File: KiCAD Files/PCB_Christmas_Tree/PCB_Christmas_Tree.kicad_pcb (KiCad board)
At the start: 2 copper layers, 207.1 x 98.8 mm, 75 parts, among them J1 Conn_01x03_Pin, J2 CR2032, J3 Conn_01x04_Pin, J4 Conn_01x04_Pin, J5 Conn_01x04_Pin, J7 Conn_01x04_Pin, Q1 AO3401A, Q2 AO3401A, Q3 AO3401A, Q4 BC817, Q5 AO3401A, SW1 SW_Omron_B3FS, U1 ATtiny402-SS

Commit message: v2 added
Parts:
- Q1: renamed from Q2; footprint Package_TO_SOT_SMD:SOT-23 -> Package_TO_SOT_SMD:SOT-323_SC-70_Handsoldering
- Q2: renamed from Q3; footprint Package_TO_SOT_SMD:SOT-23 -> Package_TO_SOT_SMD:SOT-323_SC-70_Handsoldering
- Q3: renamed from Q1; footprint Package_TO_SOT_SMD:SOT-23 -> Package_TO_SOT_SMD:SOT-323_SC-70_Handsoldering
- Q5: footprint Package_TO_SOT_SMD:SOT-23 -> Package_TO_SOT_SMD:SOT-323_SC-70_Handsoldering
- moved R5 0.13 mm to (102.6, 137.0)
- renumbered D6 to D10, D7 to D11, D8 to D12, D9 to D13, D10 to D14, D11 to D15, D12 to D16, D13 to D17, D14 to D18, D15 to D19, D23 to D2, D16 to D20, D17 to D21, D19 to D22, D20 to D23, D25 to D24, D24 to D25, D22 to D3, D21 to D4, D18 to D5, D2 to D6, D3 to D7, D4 to D8, D5 to D9, J2 to J1, J1 to J2, J7 to J3, J3 to J5, J5 to J6, R2 to R1, R7 to R10, R8 to R11, R9 to R12, R10 to R13, R11 to R14, R12 to R15, R13 to R16, R14 to R17, R15 to R18, R16 to R19, Rq1 to R2, R17 to R20, R18 to R21, R19 to R22, R20 to R23, R21 to R24, R22 to R25, R24 to R26, R25 to R27, R30 to R28, R1 to R3, R28 to R6, R27 to R7, R26 to R8, R23 to R9
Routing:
- net /LED_Power_3: track 356.2 -> 349.5 mm, vias 26 -> 24
- net /LED_Power_1: track 354.1 -> 357.6 mm
- net VDD: track 64.3 -> 66.8 mm
- net +BATT: track 34.1 -> 35.1 mm
- net Net-(Q5-G): track 5.86 -> 5.21 mm
- net Net-(D5-K): track 4.84 -> 5.43 mm
- net /LED_Power_2: track 344.6 -> 344.7 mm, vias 23 -> 22
- net GND: vias 63 -> 172
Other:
- board text added: "GND"
- board text added: "UPDI"
- board text added: "VDD"

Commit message: PCB update
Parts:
- added G***: LOGO, LOGO, F.Cu at (190.0, 130.0)
- added G***: LOGO, LOGO, B.Cu at (188.0, 134.0)
- R1, R10, R11, R12, R13, R14, R15, R16, R17, R18, R19, R2, R20, R21, R22, R23, R24, R25, R26, R27, R28, R29, R3, R4, R5, R6, R7, R8, R9: footprint Resistor_SMD:R_0603_1608Metric_Pad0.98x0.95mm_HandSolder -> Resistor_SMD:R_0805_2012Metric_Pad1.20x1.40mm_HandSolder
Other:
- outline, holes or cut-outs redrawn

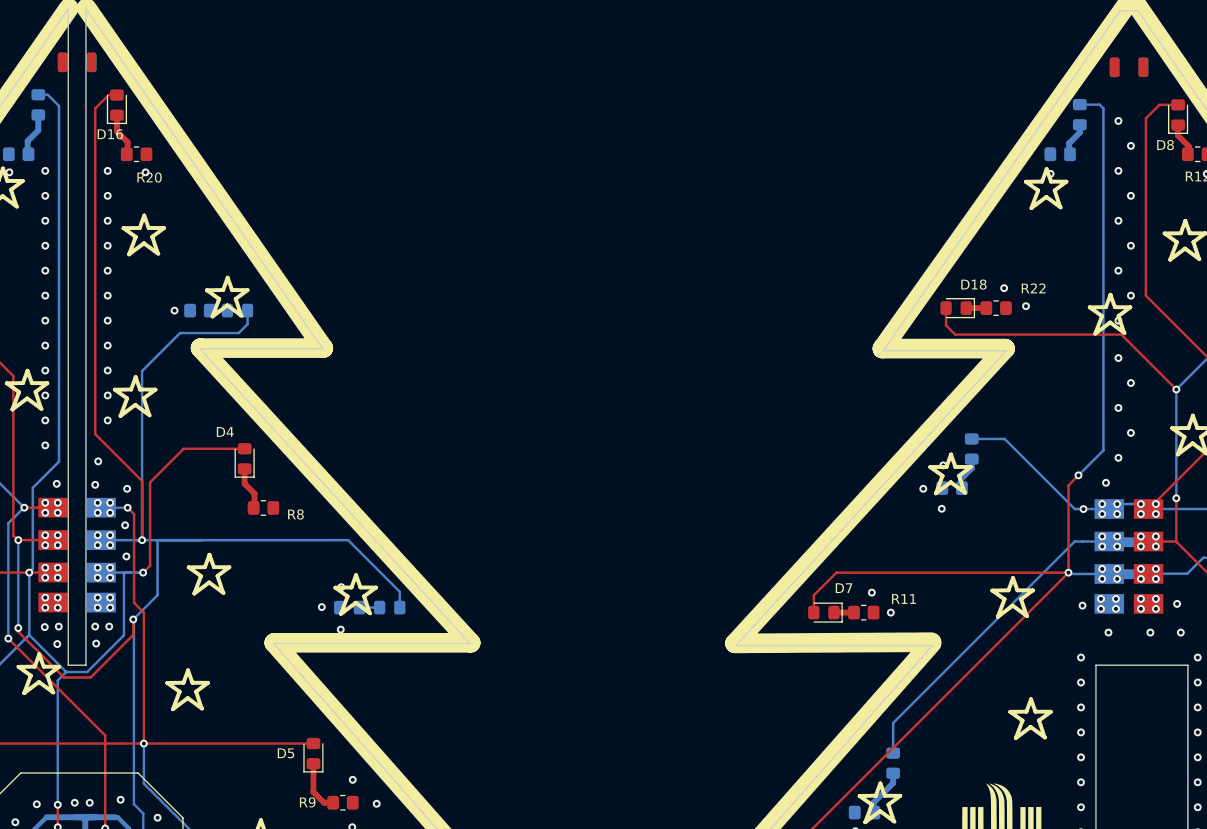
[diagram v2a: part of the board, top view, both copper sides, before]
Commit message: dodano przelotki
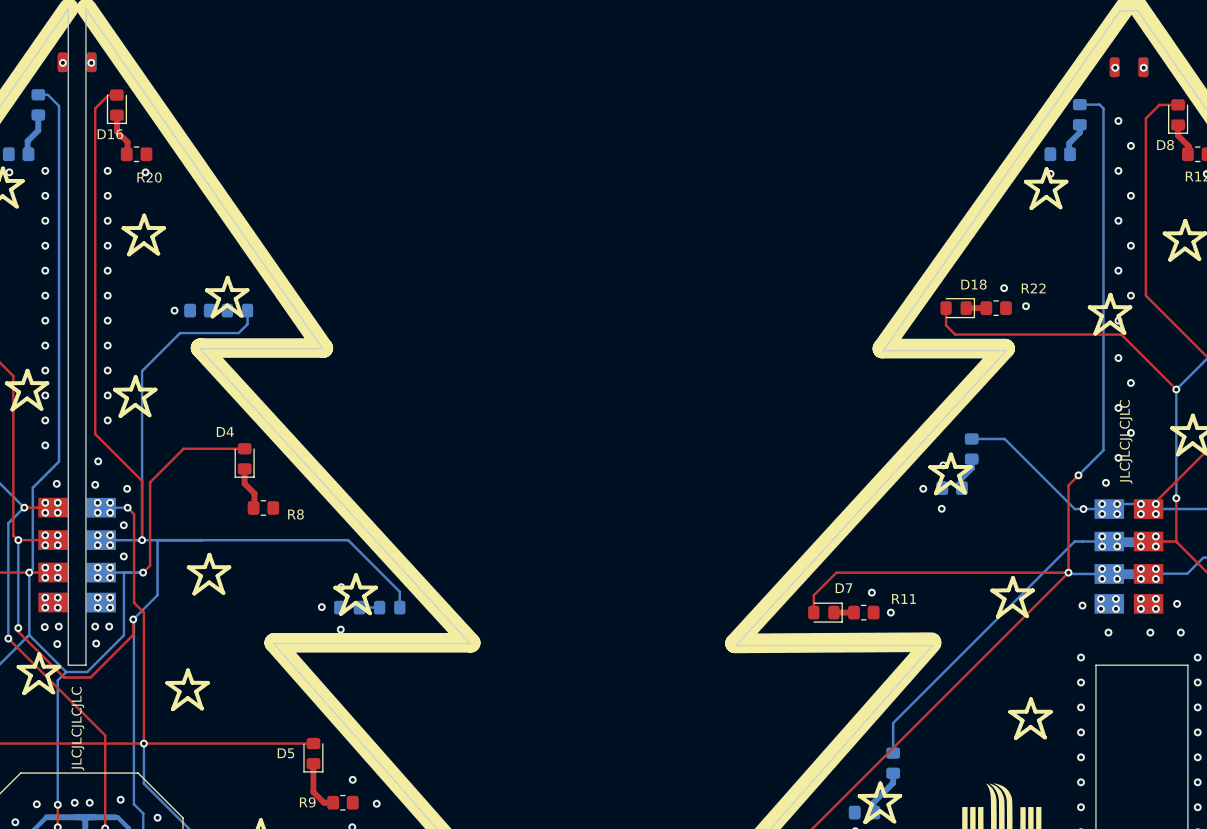
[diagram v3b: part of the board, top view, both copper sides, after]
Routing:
- net (no net): vias 0 -> 4
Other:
- board text added: "JLCJLCJLCJLC"
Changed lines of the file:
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@@
+    (effects (font (size 1 1) (thickness 0.15)) (justify left bottom))
+  )
+  (gr_text "JLCJLCJLCJLC" (at 96.52 120.65 90) (layer "F.SilkS")
     (effects (font (size 1 1) (thickness 0.15)) (justify left bottom))
   )
@@
     (effects (font (size 1 1) (thickness 0.15)) (justify left bottom))
   )
+  (gr_text "JLCJLCJLCJLC" (at 203.2 91.44 90) (layer "F.SilkS")
+    (effects (font (size 1 1) (thickness 0.15)) (justify left bottom))
+  )
   (gr_text "GND\n" (at 110.49 137.16 90) (layer "F.SilkS")
     (effects (font (size 1 1) (thickness 0.15)) (justify left bottom))
   )
+  (via (at 97.4 48.7) (size 0.8) (drill 0.4) (layers "F.Cu" "B.Cu") (net 0))
+  (via (at 201.6 49.2) (size 0.8) (drill 0.4) (layers "F.Cu" "B.Cu") (net 0))
+  (via (at 94.5 48.7) (size 0.8) (drill 0.4) (layers "F.Cu" "B.Cu") (net 0))
+  (via (at 204.5 49.2) (size 0.8) (drill 0.4) (layers "F.Cu" "B.Cu") (net 0))
   (segment (start 94.696 132.6455) (end 95.4005 133.35) (width 0.45) (layer "B.Cu") (net 1))
   (segment (start 94.696 130.6945) (end 94.696 132.6455) (width 0.45) (layer "B.Cu") (net 1))
@@
   (via (at 124.0028 121.666) (size 0.8) (drill 0.4) (layers "F.Cu" "B.Cu") (free) (net 24))
   (via (at 99.314 104.14) (size 0.8) (drill 0.4) (layers "F.Cu" "B.Cu") (net 24))
-  (via (at 100.838 95.758) (size 0.8) (drill 0.4) (layers "F.Cu" "B.Cu") (free) (net 24))
+  (via (at 100.7 95.758) (size 0.8) (drill 0.4) (layers "F.Cu" "B.Cu") (free) (net 24))
   (via (at 210 111.76) (size 0.8) (drill 0.4) (layers "F.Cu" "B.Cu") (free) (net 24))
   (via (at 198.12 137.16) (size 0.8) (drill 0.4) (layers "F.Cu" "B.Cu") (free) (net 24))
@@
   (via (at 210 114.3) (size 0.8) (drill 0.4) (layers "F.Cu" "B.Cu") (free) (net 24))
   (via (at 81.1276 131.5212) (size 0.8) (drill 0.4) (layers "F.Cu" "B.Cu") (free) (net 24))
-  (via (at 100.965 98.933) (size 0.8) (drill 0.4) (layers "F.Cu" "B.Cu") (free) (net 24))
+  (via (at 100.7 98.933) (size 0.8) (drill 0.4) (layers "F.Cu" "B.Cu") (free) (net 24))
   (via (at 230.9368 121.92) (size 0.8) (drill 0.4) (layers "F.Cu" "B.Cu") (free) (net 24))
   (via (at 200.152 104.267) (size 0.8) (drill 0.4) (layers "F.Cu" "B.Cu") (net 24))

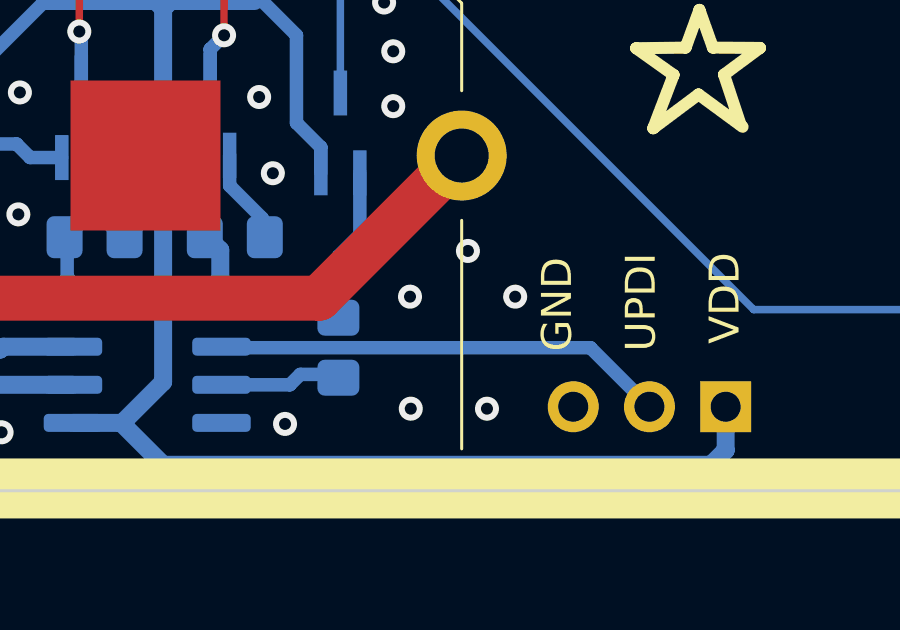
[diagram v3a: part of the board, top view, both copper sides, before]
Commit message: zmiana pinoutu zlacza UPDI
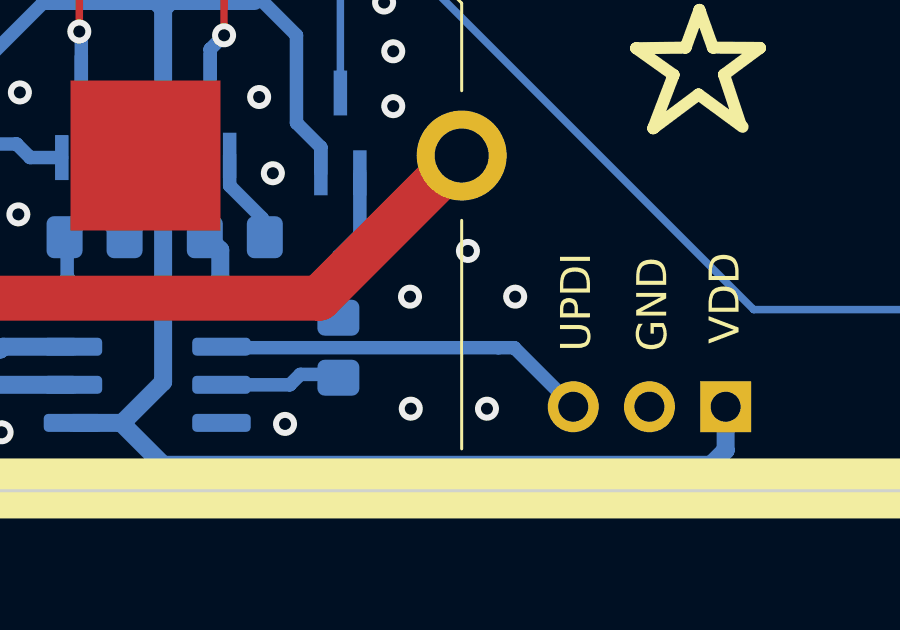
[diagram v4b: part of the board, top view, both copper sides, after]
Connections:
- J2 pad 2: /UDPI -> GND
- J2 pad 3: GND -> /UDPI
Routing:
- net /UDPI: track 15.1 -> 12.6 mm
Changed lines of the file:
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@@
       (net 23 "VDD") (pinfunction "Pin_1") (pintype "passive"))
     (pad "2" thru_hole oval (at 0 -2.54 90) (size 1.7 1.7) (drill 1) (layers "*.Cu" "*.Mask")
-      (net 42 "/UDPI") (pinfunction "Pin_2") (pintype "passive"))
+      (net 24 "GND") (pinfunction "Pin_2") (pintype "passive"))
     (pad "3" thru_hole oval (at 0 -5.08 90) (size 1.7 1.7) (drill 1) (layers "*.Cu" "*.Mask")
-      (net 24 "GND") (pinfunction "Pin_3") (pintype "passive"))
+      (net 42 "/UDPI") (pinfunction "Pin_3") (pintype "passive"))
     (model "${KICAD6_3DMODEL_DIR}/Connector_PinHeader_2.54mm.3dshapes/PinHeader_1x03_P2.54mm_Vertical.wrl"
       (offset (xyz 0 0 0))
@@
     (effects (font (size 1 1) (thickness 0.15)) (justify left bottom))
   )
-  (gr_text "UPDI" (at 113.284 137.16 90) (layer "F.SilkS")
+  (gr_text "UPDI" (at 111.125 137.16 90) (layer "F.SilkS")
     (effects (font (size 1 1) (thickness 0.15)) (justify left bottom))
   )
@@
     (effects (font (size 1 1) (thickness 0.15)) (justify left bottom))
   )
-  (gr_text "GND\n" (at 110.49 137.16 90) (layer "F.SilkS")
+  (gr_text "GND\n" (at 113.665 137.16 90) (layer "F.SilkS")
     (effects (font (size 1 1) (thickness 0.15)) (justify left bottom))
   )
@@
   (segment (start 111.243 73.914) (end 109.3615 73.914) (width 0.25) (layer "B.Cu") (net 40))
   (segment (start 233.163 104.902) (end 230.1005 104.902) (width 0.6) (layer "B.Cu") (net 41))
+  (segment (start 98.753 137.033) (end 107.95 137.033) (width 0.45) (layer "B.Cu") (net 42))
   (segment (start 98.719 136.999) (end 98.753 137.033) (width 0.45) (layer "B.Cu") (net 42))
-  (segment (start 111.018 137.033) (end 112.985 139) (width 0.45) (layer "B.Cu") (net 42))
-  (segment (start 98.753 137.033) (end 111.018 137.033) (width 0.45) (layer "B.Cu") (net 42))
+  (segment (start 108.478 137.033) (end 107.95 137.033) (width 0.45) (layer "B.Cu") (net 42))
+  (segment (start 110.445 139) (end 108.478 137.033) (width 0.45) (layer "B.Cu") (net 42))
   (zone (net 24) (net_name "GND") (layers "F&B.Cu") (hatch edge 0.5)
     (connect_pads (clearance 0.5))
